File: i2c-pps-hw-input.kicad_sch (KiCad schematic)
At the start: 0 parts

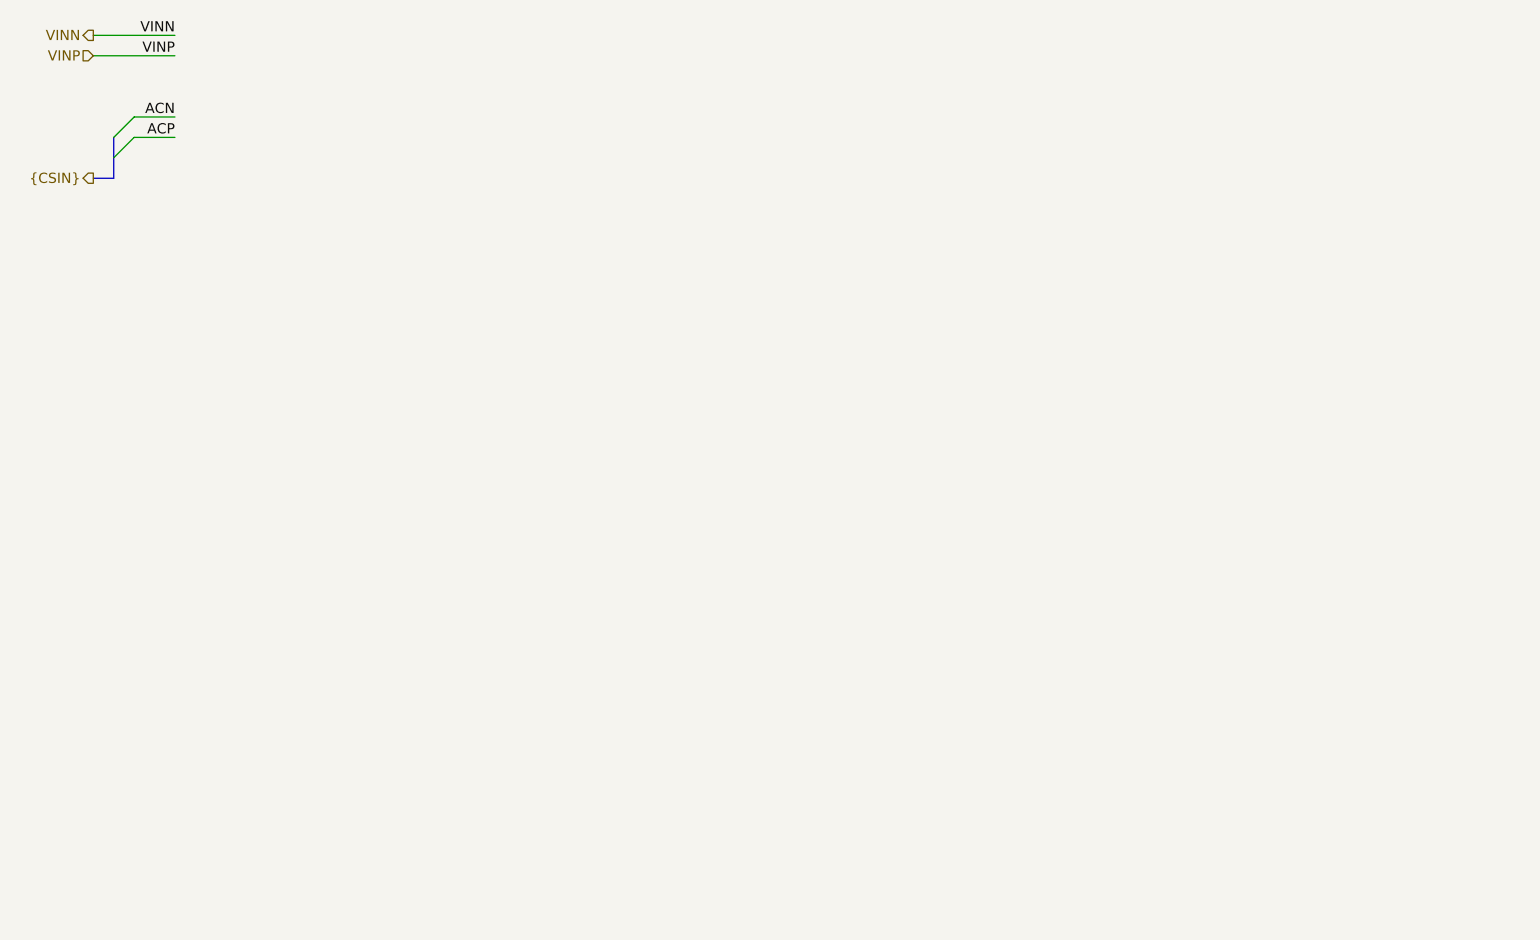
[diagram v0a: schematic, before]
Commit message: Design schematics and set per component requirements
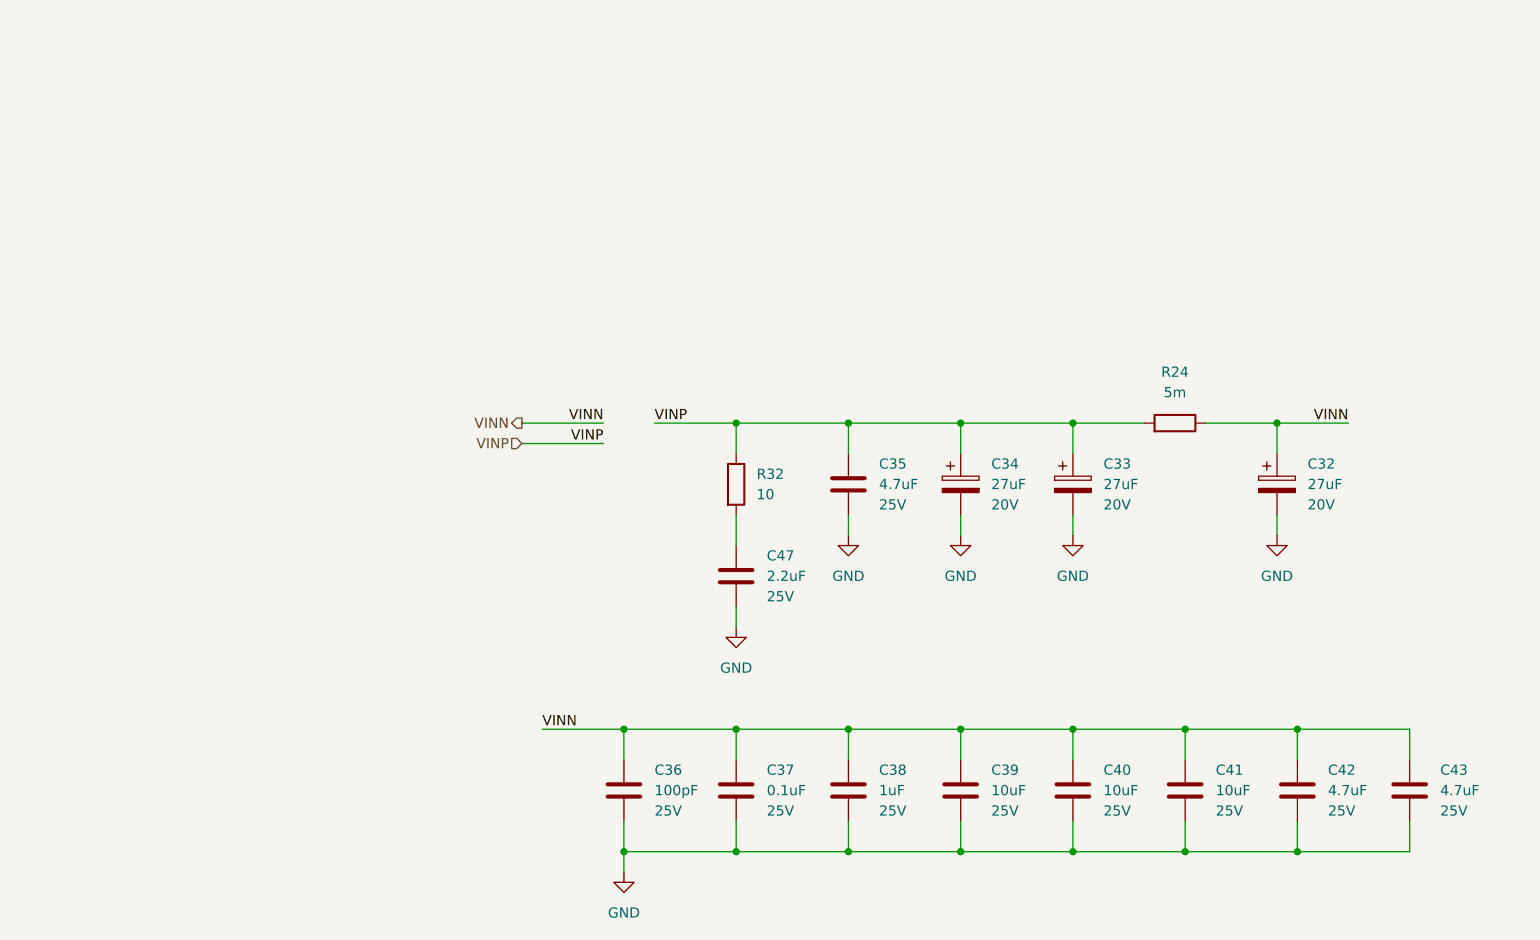
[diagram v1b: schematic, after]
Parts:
- added C32, C33, C34: 27uF, Capacitor_SMD:C_Elec_10x10.2, symbol Device:C_Polarized
- added C35, C42, C43: 4.7uF, Capacitor_SMD:C_1210_3225Metric, symbol Device:C
- added C36: 100pF, Capacitor_SMD:C_0603_1608Metric_Pad1.08x0.95mm_HandSolder, symbol Device:C
- added C37: 0.1uF, Capacitor_SMD:C_0603_1608Metric_Pad1.08x0.95mm_HandSolder, symbol Device:C
- added C38: 1uF, Capacitor_SMD:C_0805_2012Metric, symbol Device:C
- added C39, C40, C41: 10uF, Capacitor_SMD:C_1210_3225Metric, symbol Device:C
- added C47: 2.2uF, Capacitor_SMD:C_1210_3225Metric, symbol Device:C
- added R24: 5m, Resistor_SMD:R_1206_3216Metric, symbol Device:R
- added R32: 10, Resistor_SMD:R_1206_3216Metric, symbol Device:R
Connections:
- net VINN: now also C32.1, C36.1, C37.1, C38.1, C39.1, C40.1, C41.1, C42.1, C43.1, R24.1
- net VINP: now also C33.1, C34.1, C35.1, R24.2, R32.1
- new net: C47.1, R32.2
- new net GND: C32.2, C33.2, C34.2, C35.2, C36.2, C37.2, C38.2, C39.2, C40.2, C41.2, C42.2, C43.2, C47.2

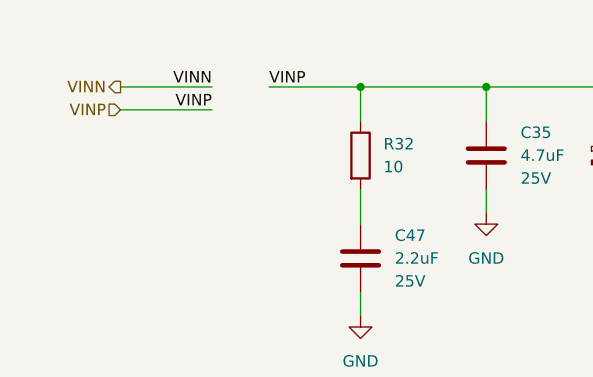
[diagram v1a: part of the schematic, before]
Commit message: Rename VINP to +5V_Run for clarity
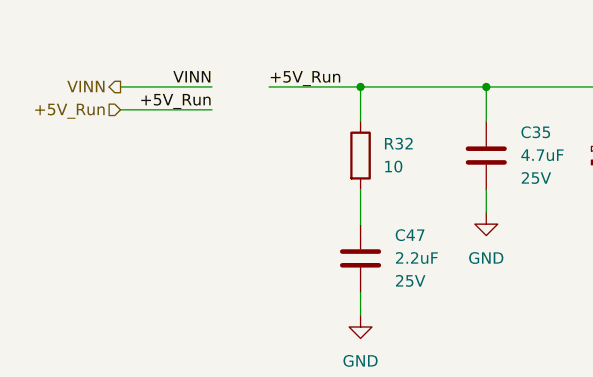
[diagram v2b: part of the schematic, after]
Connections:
- net VINP renamed +5V_Run
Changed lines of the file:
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@@
 		)
 	)
-	(label "VINP"
+	(label "+5V_Run"
 		(at 88.9 76.2 180)
 		(effects
@@
 		)
 	)
-	(label "VINP"
+	(label "+5V_Run"
 		(at 95.25 73.66 0)
 		(effects
@@
 		)
 	)
-	(hierarchical_label "VINP"
+	(hierarchical_label "+5V_Run"
 		(shape input)
 		(at 78.74 76.2 180)

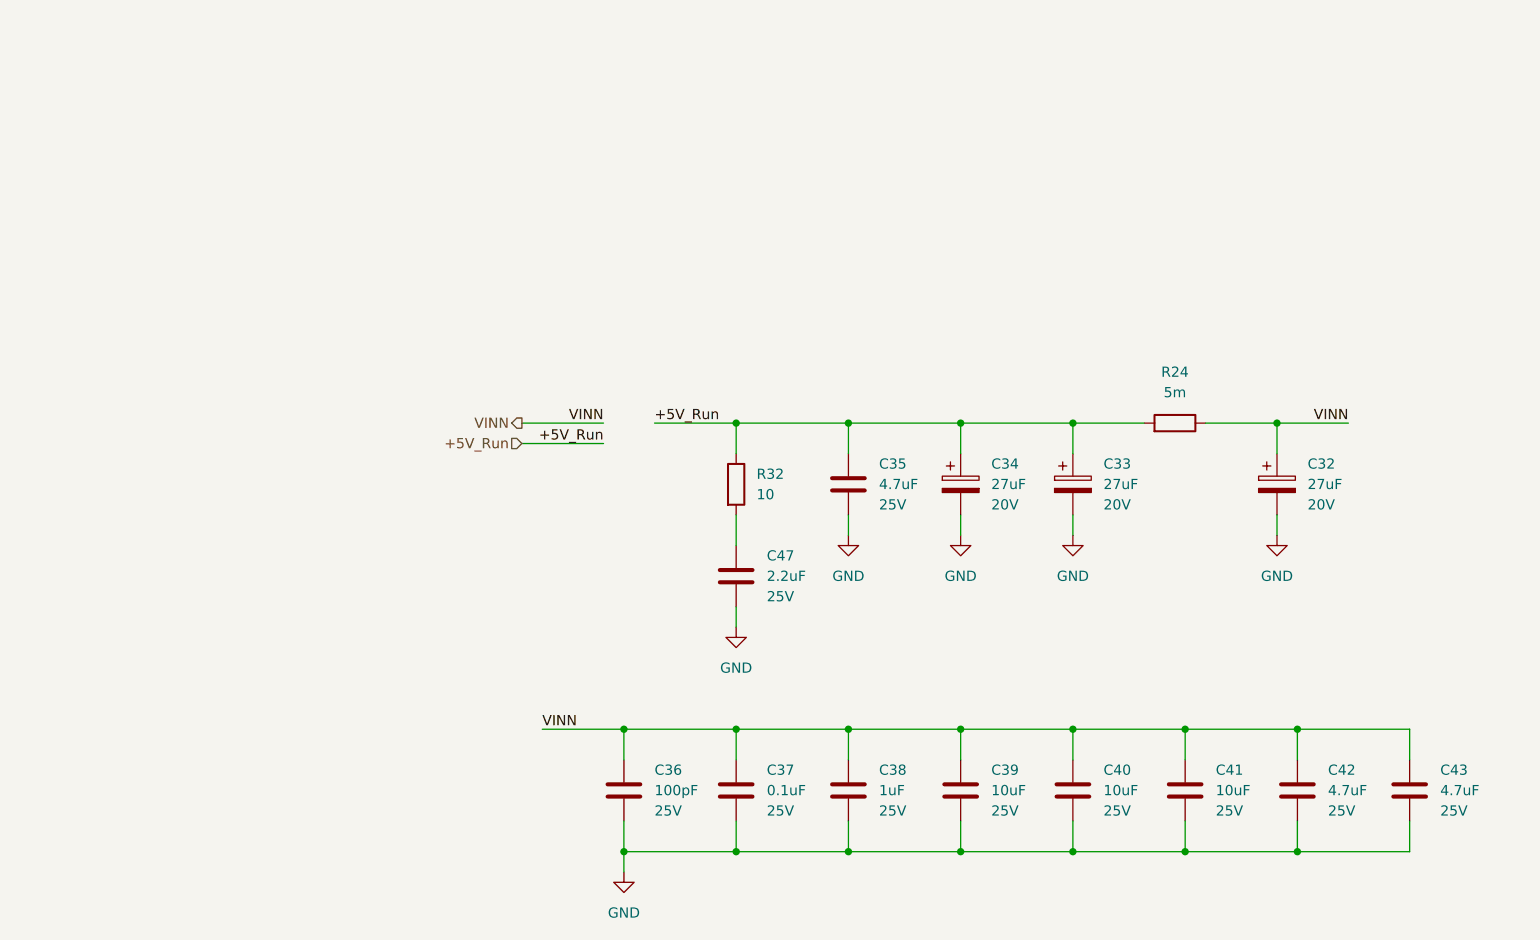
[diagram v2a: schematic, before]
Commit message: Rename VINN to +5V_Filtered for clarity
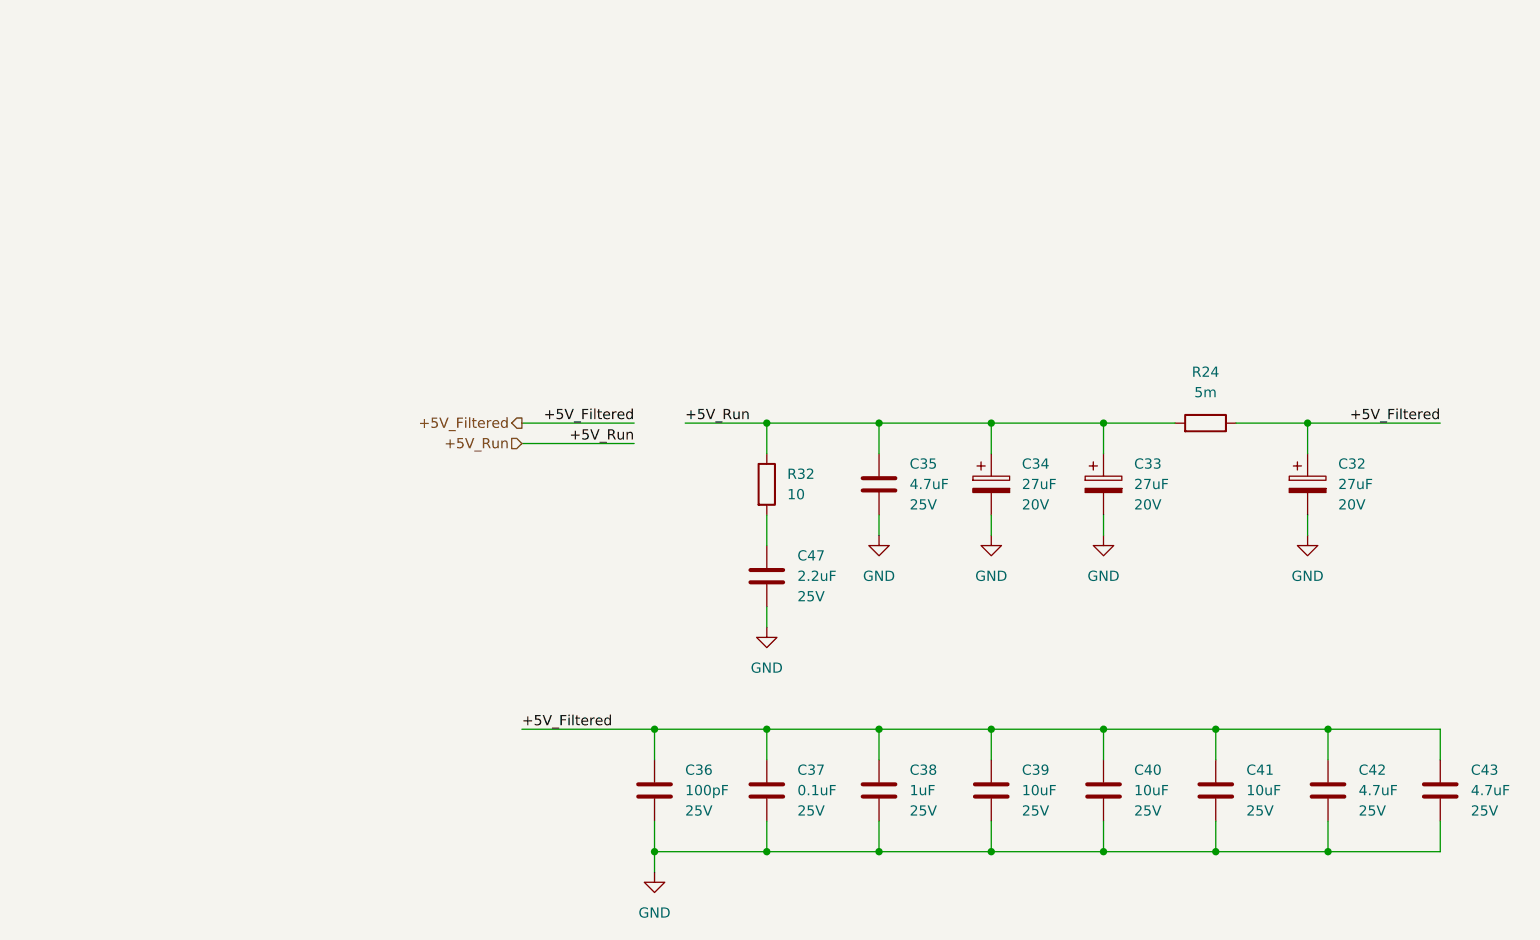
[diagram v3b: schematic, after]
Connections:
- net VINN renamed +5V_Filtered
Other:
- moved on the sheet: C32, C33, C34, C35, C36, C37, C38, C39, C40, C41, C42, C43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

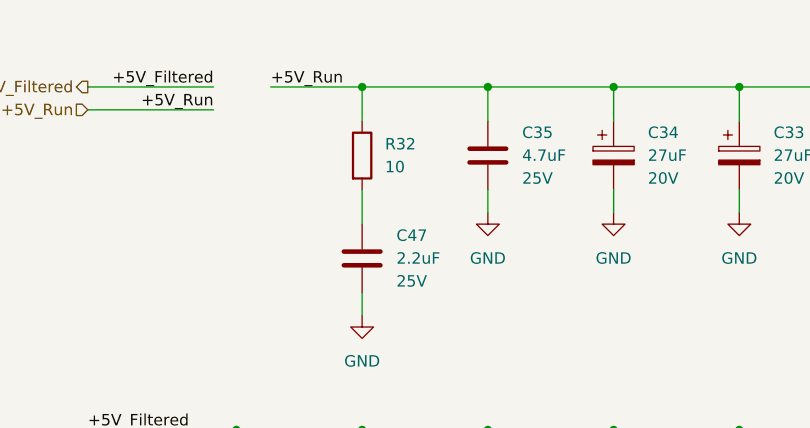
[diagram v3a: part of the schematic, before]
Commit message: Add more indicator LEDs
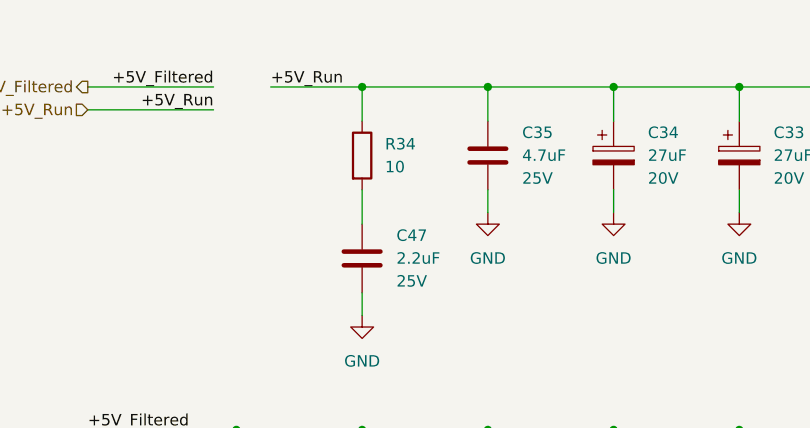
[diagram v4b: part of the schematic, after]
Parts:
- renumbered R32 to R34
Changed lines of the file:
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@@
 		(dnp no)
 		(fields_autoplaced yes)
-		(property "Reference" "R32"
+		(property "Reference" "R34"
 			(at 111.76 80.0099 0)
 			(effects
@@
 			(project ""
 				(path "/512c4d3f-92f6-4670-bf9b-2123d46bbde3/bfa8dadb-54f9-4e18-b93b-6165b820488c"
-					(reference "R32")
+					(reference "R34")
 					(unit 1)
 				)

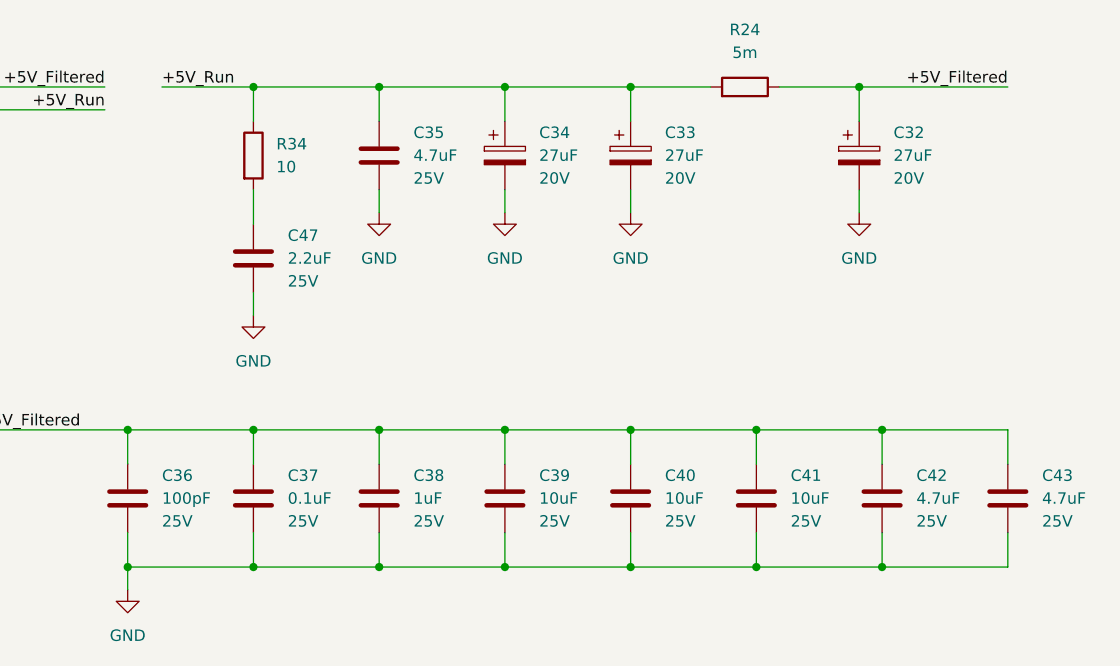
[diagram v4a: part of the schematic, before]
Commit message: Select market available components
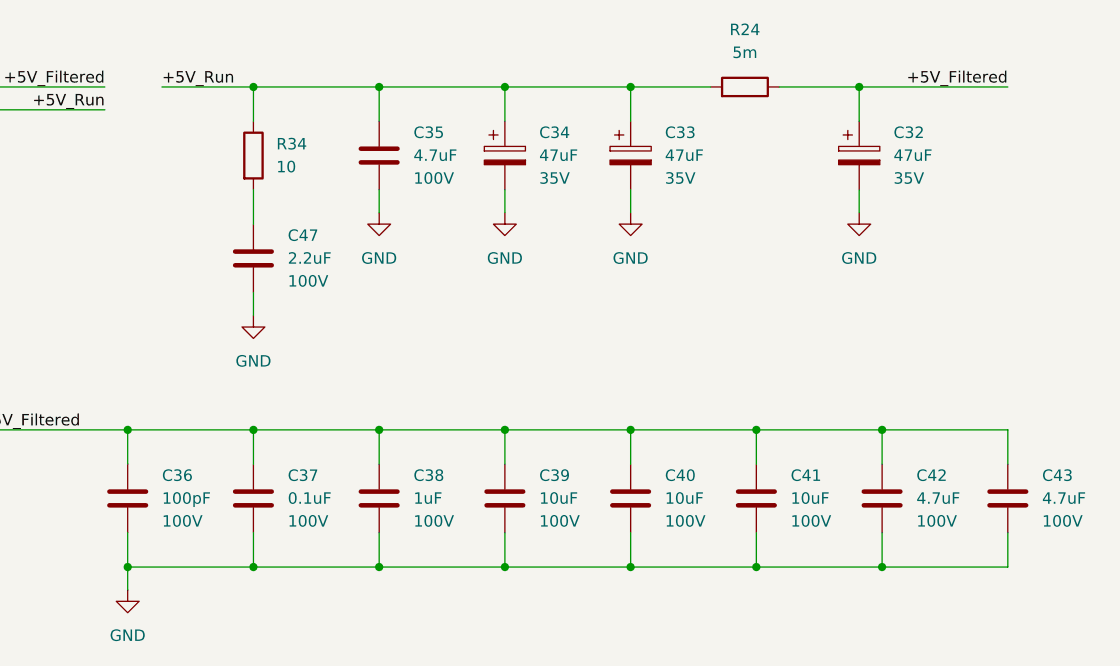
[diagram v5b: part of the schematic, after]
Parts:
- C32, C33, C34: value 27uF -> 47uF; footprint Capacitor_SMD:C_Elec_10x10.2 -> Capacitor_SMD:CP_Elec_6.3x5.7; Manufacturer (none) -> KEMET; Part Number (none) -> A768EB476M1VLAE042; Rated Voltage 20V -> 35V
- C35, C42, C43: Manufacturer (none) -> Murata Electronics; Part Number (none) -> GCJ32DC72A475KE01L; Rated Voltage 25V -> 100V
- C36: Manufacturer (none) -> TDK Corporation; Part Number (none) -> CGA3E2C0G2A101J080AA; Rated Voltage 25V -> 100V
- C37: Manufacturer (none) -> Taiyo Yuden; Part Number (none) -> HMK107B7104KAHT; Rated Voltage 25V -> 100V
- C38: Manufacturer (none) -> KYOCERA AVX; Part Number (none) -> 08051C105K4Z2A; Rated Voltage 25V -> 100V
- C39, C40, C41: Manufacturer (none) -> TDK Corporation; Part Number (none) -> C3225X7R2A106K250AC; Rated Voltage 25V -> 100V
- C47: Manufacturer (none) -> TDK Corporation; Part Number (none) -> CGA6N3X7R2A225K230AE; Rated Voltage 25V -> 100V
- R24: footprint Resistor_SMD:R_1206_3216Metric -> Resistor_SMD:R_2512_6332Metric; Manufacturer (none) -> YAGEO; Part Number (none) -> PA2512FKM070R005E
- R34: Manufacturer (none) -> YAGEO; Part Number (none) -> SR1206FR-7T10RL
